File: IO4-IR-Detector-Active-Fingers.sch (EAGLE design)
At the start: 48 parts, among them J1 0.100, J10 0.100, J11 0.100, J12 0.100, J13 0.100, J14 0.100, J15 0.100, J16 0.100, J2 0.100, J3 0.100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

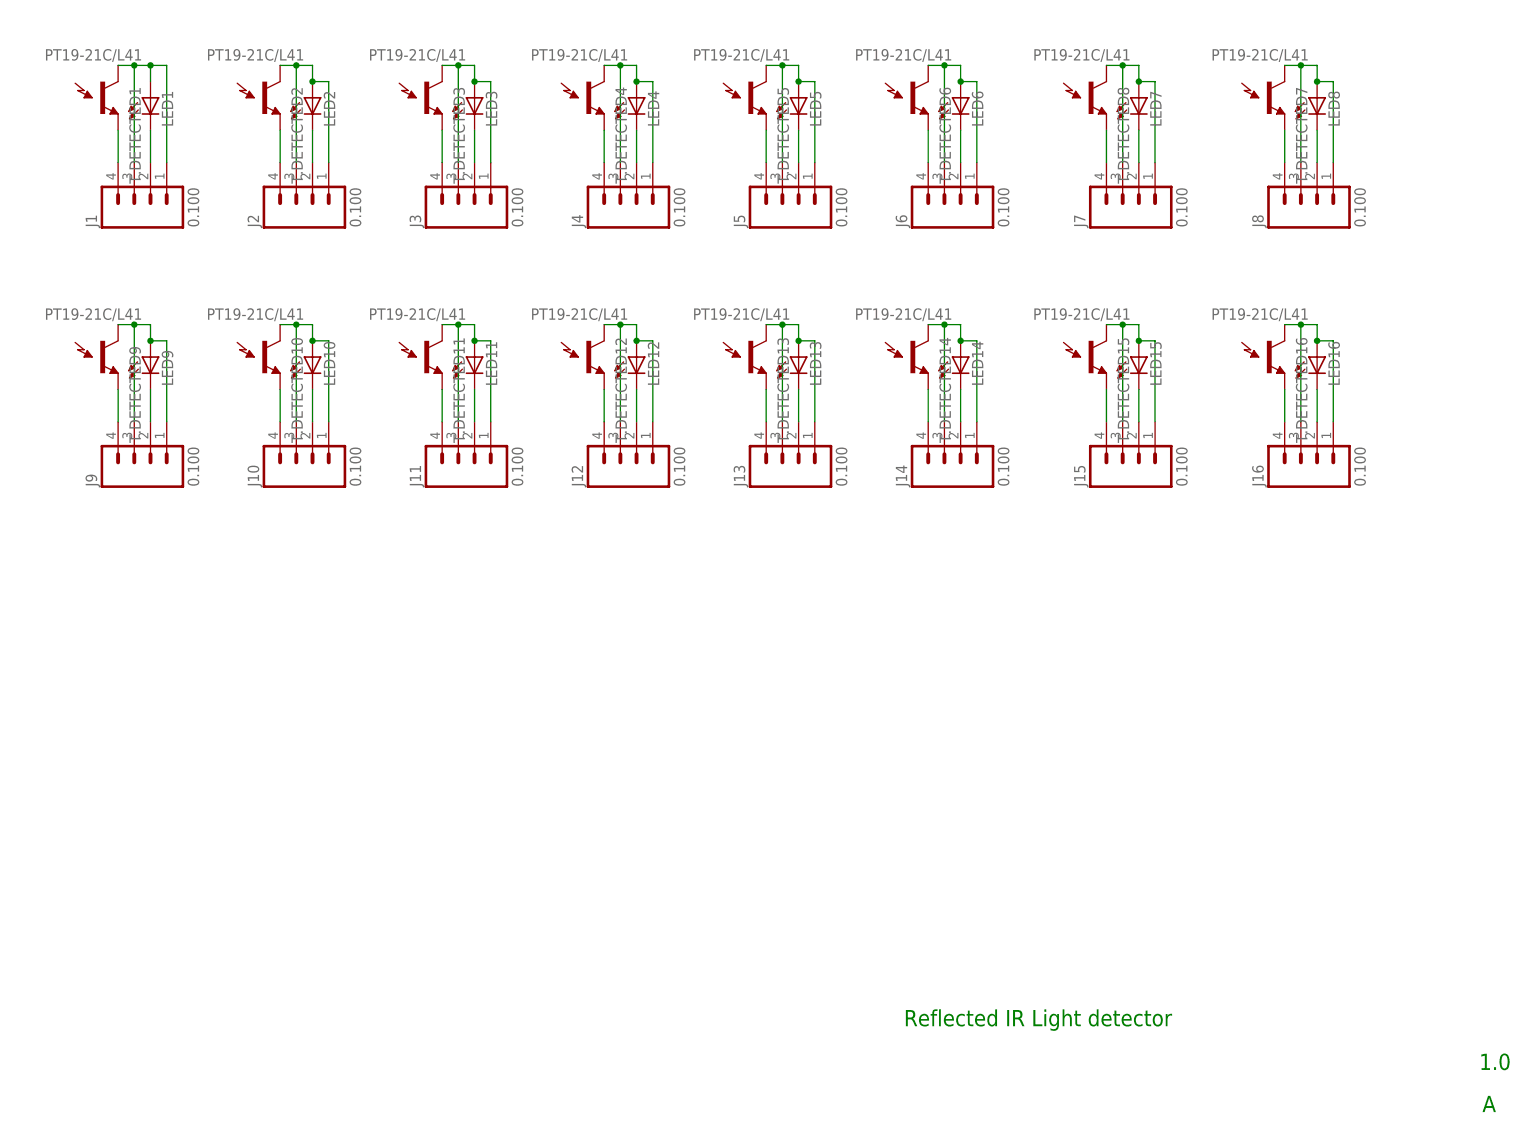
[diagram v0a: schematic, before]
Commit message: JLC requires 6mm board width, switch to QRE1113GR
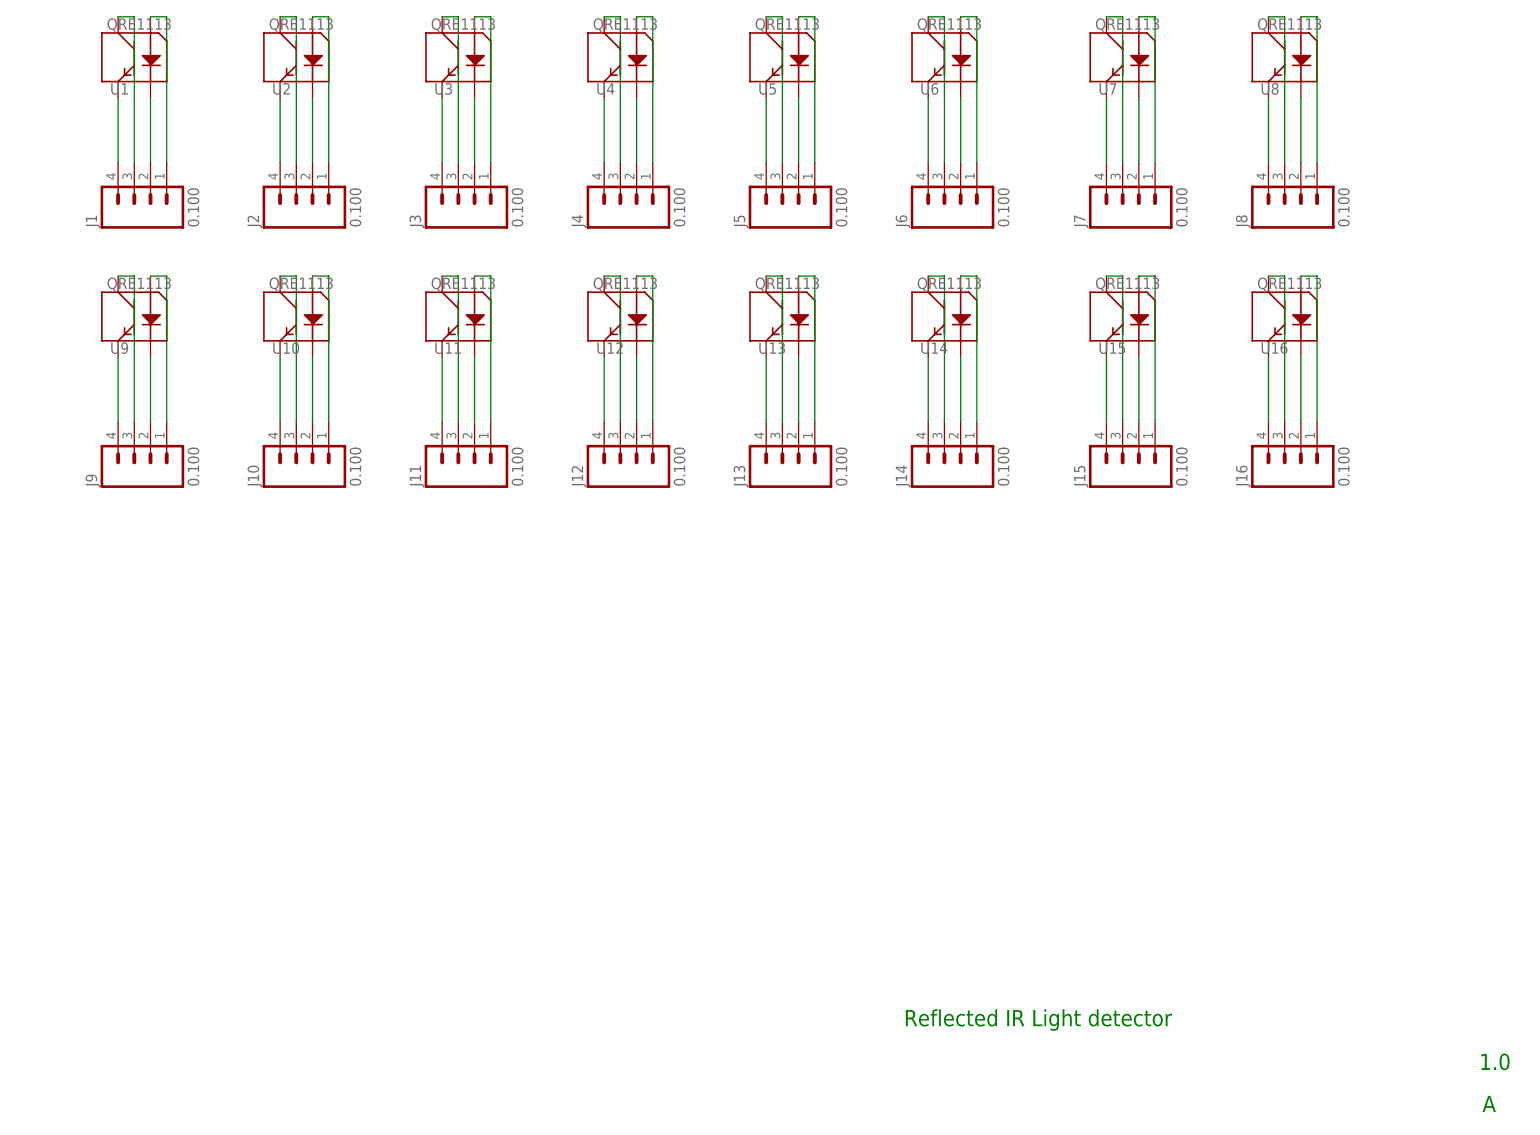
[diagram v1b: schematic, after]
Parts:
- removed LED1, LED10, LED11, LED12, LED13, LED14, LED15, LED16, LED2, LED3, LED4, LED5, LED6, LED7, LED8, LED9: (no value), SPCoast:LED0603-LED
- removed T.DETECTED1, T.DETECTED10, T.DETECTED11, T.DETECTED12, T.DETECTED13, T.DETECTED14, T.DETECTED15, T.DETECTED16, T.DETECTED2, T.DETECTED3, T.DETECTED4, T.DETECTED5, T.DETECTED6, T.DETECTED7, T.DETECTED8, T.DETECTED9: PT19-21C/L41, SPCoast:LIGHTSENSORALS
- added U1, U10, U11, U12, U13, U14, U15, U16, U2, U3, U4, U5, U6, U7, U8, U9: QRE1113, SPCoast:QRE1113
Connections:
- new net N$12: J10.1, U10.A
- new net N$16: J14.1, U14.A
- new net N$20: J2.2, U2.K
- new net N$24: J3.1, U3.A
- new net N$28: J5.1, U5.A
- new net N$32: J7.4, U7.E
- new net N$4: J4.4, U4.E
- new net N$57: J14.2, U14.K
- new net N$58: J15.4, U15.E
- new net N$59: J15.2, U15.K
- new net N$60: J16.4, U16.E
- new net N$61: J16.2, U16.K
- new net N$62: J10.3, U10.C
- new net N$63: J9.3, U9.C
- new net N$64: J6.3, U6.C
- new net N$8: J6.1, U6.A
- net N$1: now also U1.E; no longer T.DETECTED1.E1
- net N$10: now also J8.1, U8.A; no longer J3.1, J3.3, LED3.A, T.DETECTED3.C1
- net N$11: now also J9.1, U9.A; no longer J3.2, LED3.C
- net N$13: now also J11.1, U11.A; no longer J4.4, T.DETECTED4.E1
- net N$14: now also J12.1, U12.A; no longer J4.1, J4.3, LED4.A, T.DETECTED4.C1
- net N$15: now also J13.1, U13.A; no longer J4.2, LED4.C
- net N$17: now also J15.1, U15.A; no longer J5.4, T.DETECTED5.E1
- net N$18: now also J16.1, U16.A; no longer J5.1, J5.3, LED5.A, T.DETECTED5.C1
- net N$19: now also J2.4, U2.E; no longer J5.2, LED5.C
- net N$2: now also U1.K; no longer LED1.C
- net N$21: now also J2.1, U2.A; no longer J6.4, T.DETECTED6.E1
- net N$22: now also J3.4, U3.E; no longer J6.1, J6.3, LED6.A, T.DETECTED6.C1
- net N$23: now also J3.2, U3.K; no longer J6.2, LED6.C
- net N$25: now also J2.3, U2.C; no longer J8.4, T.DETECTED7.E1
- net N$26: now also J5.4, U5.E; no longer J8.2, LED8.C
- net N$27: now also J5.2, U5.K; no longer J8.1, J8.3, LED8.A, T.DETECTED7.C1
- net N$29: now also J6.4, U6.E; no longer J7.4, T.DETECTED8.E1
- net N$3: now also U1.A; no longer J1.3, LED1.A, T.DETECTED1.C1
- net N$30: now also J6.2, U6.K; no longer J7.2, LED7.C
- net N$31: now also J3.3, U3.C; no longer J7.1, J7.3, LED7.A, T.DETECTED8.C1
- net N$33: now also J7.2, U7.K; no longer J9.4, T.DETECTED9.E1
- net N$34: now also J4.3, U4.C; no longer J9.1, J9.3, LED9.A, T.DETECTED9.C1
- net N$35: now also J8.4, U8.E; no longer J10.4, T.DETECTED10.E1
- net N$36: now also J8.2, U8.K; no longer J10.1, J10.3, LED10.A, T.DETECTED10.C1
- net N$37: now also J5.3, U5.C; no longer J11.4, T.DETECTED11.E1
- net N$38: now also J9.4, U9.E; no longer J11.1, J11.3, LED11.A, T.DETECTED11.C1
- net N$39: now also J9.2, U9.K; no longer J12.4, T.DETECTED12.E1
- net N$40: now also J7.3, U7.C; no longer J12.1, J12.3, LED12.A, T.DETECTED12.C1
- net N$41: now also J8.3, U8.C; no longer J13.4, T.DETECTED13.E1
- net N$42: now also J16.3, U16.C; no longer J13.1, J13.3, LED13.A, T.DETECTED13.C1
- net N$43: now also J15.3, U15.C; no longer J14.4, T.DETECTED14.E1
- net N$44: now also U14.C; no longer J14.1, LED14.A, T.DETECTED14.C1
- net N$45: now also J10.4, U10.E; no longer J15.4, T.DETECTED15.E1
- net N$46: now also J10.2, U10.K; no longer J15.1, J15.3, LED15.A, T.DETECTED15.C1
- net N$47: now also J13.3, U13.C; no longer J16.4, T.DETECTED16.E1
- net N$48: now also J11.4, U11.E; no longer J16.1, J16.3, LED16.A, T.DETECTED16.C1
- net N$49: now also J11.2, U11.K; no longer J9.2, LED9.C
- net N$5: now also J4.2, U4.K; no longer J2.4, T.DETECTED2.E1
- net N$50: now also J12.3, U12.C; no longer J10.2, LED10.C
- net N$51: now also J12.4, U12.E; no longer J11.2, LED11.C
- net N$52: now also U12.K; no longer LED12.C
- net N$53: now also J13.4, U13.E; no longer J13.2, LED13.C
- net N$54: now also J13.2, U13.K; no longer J14.2, LED14.C
- net N$55: now also J11.3, U11.C; no longer J15.2, LED15.C
- net N$56: now also J14.4, U14.E; no longer J16.2, LED16.C
- net N$6: now also J4.1, U4.A; no longer J2.1, J2.3, LED2.A, T.DETECTED2.C1
- net N$7: now also J1.3, U1.C; no longer J2.2, LED2.C
- net N$9: now also J7.1, U7.A; no longer J3.4, T.DETECTED3.E1
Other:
- moved on the sheet: J16, J8
